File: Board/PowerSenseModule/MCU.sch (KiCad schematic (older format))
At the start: 38 parts, among them J3 Programming Header, J4 Conn_01x02_Male, U2 NCV2007x, U3 dsPIC33EV32GM102, U4 MCP2542FDxMF, Y1 Crystal

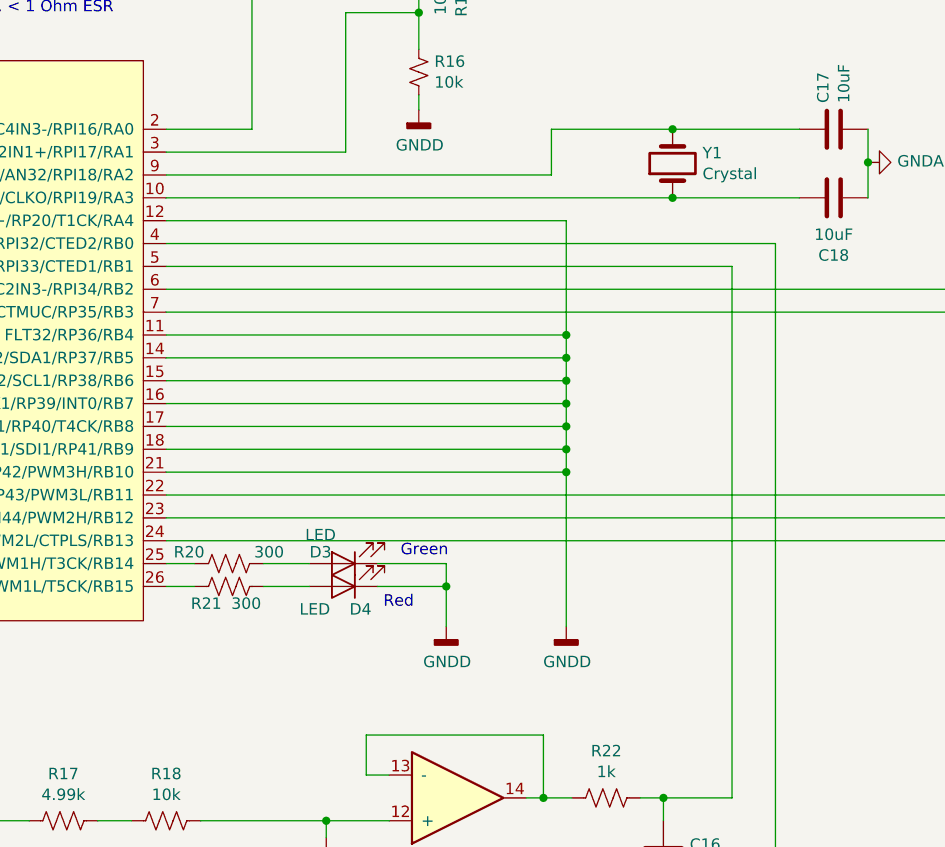
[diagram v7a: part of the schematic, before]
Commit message: Updated symbol fields and changed CAN transceiver package to make it easier to solder
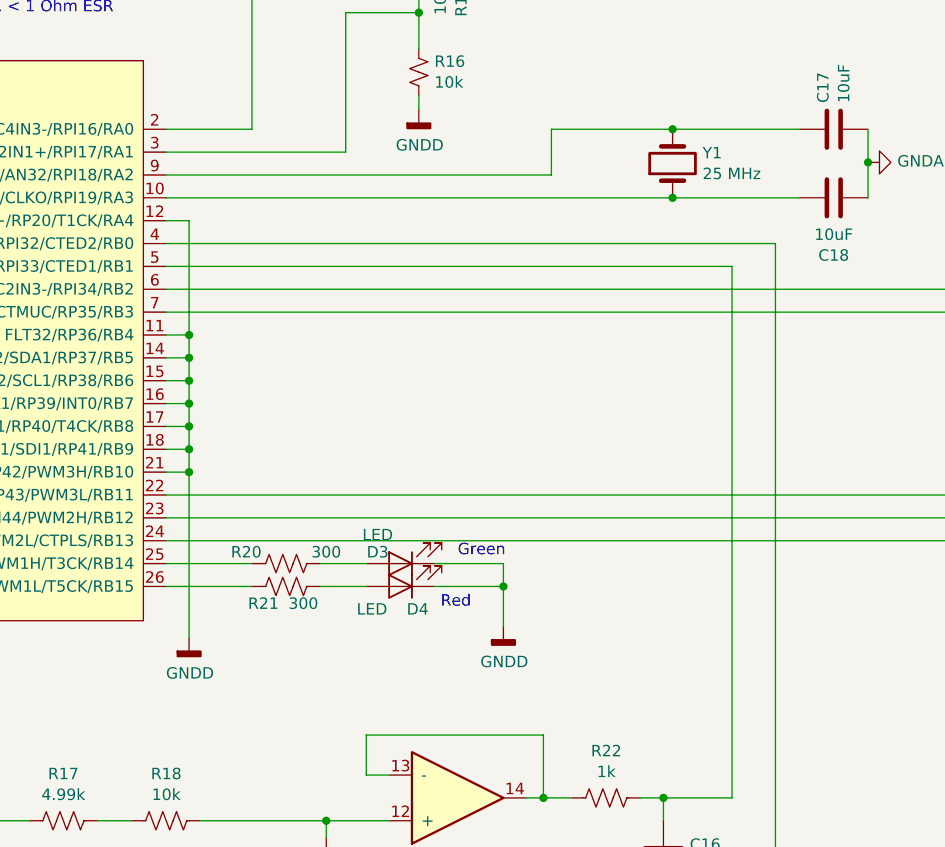
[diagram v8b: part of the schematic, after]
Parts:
- R8: footprint Resistor_SMD:R_2512_6332Metric_Pad1.52x3.35mm_HandSolder -> Resistor_SMD:R_4020_10251Metric_Pad1.65x5.30mm_HandSolder; Manufacturer (none) -> Vishay; Manufacturer PN (none) -> WSLP39214L000FEB; Supplier (none) -> Mouser; Supplier Link (none) -> https://www.mouser.com/ProductDetail/Vishay-Dale/WSLP39214L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; Supplier PN (none) -> 71- 71-WSLP39214L000FEB
- U2: Manufacturer (none) -> ON Semiconductor; Manufacturer PN (none) -> NCV20074DR2G; Price 1 QTY (none) -> 1.19; Supplier (none) -> Mouser; Supplier Link (none) -> https://www.mouser.com/ProductDetail/ON-Semiconductor/NCV20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; Supplier PN (none) -> 863-NCV20074DR2G
- U3: Manufacturer (none) -> Microchip; Manufacturer PN (none) -> dsPIC33EV32GM102-E/SS; Price 1 QTY (none) -> 3.04; Supplier (none) -> Mouser; Supplier Link (none) -> https://www.mouser.com/ProductDetail/Microchip-Technology/d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; Supplier PN (none) -> 579-33EV32GM102ESS
- U4: footprint Package_DFN_QFN:DFN-8-1EP_3x3mm_P0.65mm_EP1.55x2.4mm -> Package_SO:SOIC-8_3.9x4.9mm_P1.27mm; Manufacturer (none) -> Microchip; Manufacturer PN (none) -> MCP2542FD-H/SN; Price 1 QTY (none) -> 0.79; Supplier (none) -> Mouser; Supplier Link (none) -> https://www.mouser.com/ProductDetail/Microchip-Technology/M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; Supplier PN (none) -> 579-MCP2542FD-H/SN
- Y1: value Crystal -> 25 MHz; Manufacturer (none) -> Abracon; Manufacturer PN (none) -> ABM10AIG-25.000MHZ-4Z-T3; Price 1 QTY (none) -> 1.30; Supplier (none) -> Mouser; Supplier Link (none) -> https://www.mouser.com/ProductDetail/ABRACON/ABM10AIG-25000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; Supplier PN (none) -> 815-M10AIG-25-4ZT3
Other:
- moved on the sheet: D3, D4, R20, R21
